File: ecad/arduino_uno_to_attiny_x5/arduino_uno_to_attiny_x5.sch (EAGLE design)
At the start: 3 parts

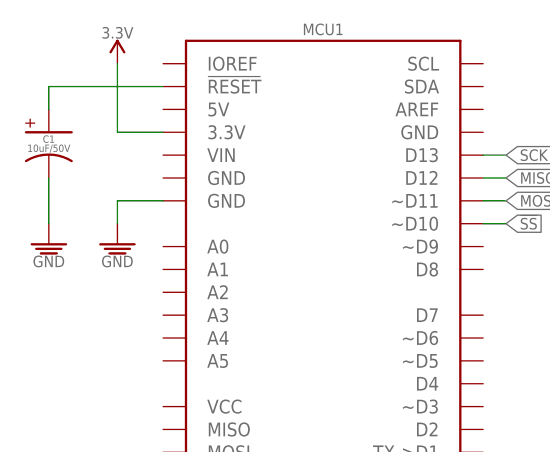
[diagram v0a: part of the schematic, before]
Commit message: Create schematic for pocket avr programmer (AVR ISP header) to ATtiny85.  Updated all schematics and their respective images.
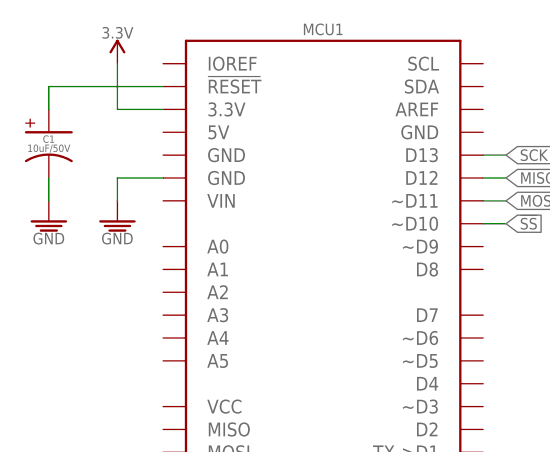
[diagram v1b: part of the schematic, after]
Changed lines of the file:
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@@
 <?xml version="1.0" encoding="utf-8"?>
 <!DOCTYPE eagle SYSTEM "eagle.dtd">
-<eagle version="9.1.1">
+<eagle version="9.1.3">
 <drawing>
 <settings>
@@
 <setting verticaltext="up"/>
 </settings>
-<grid distance="0.1" unitdist="inch" unit="inch" style="lines" multiple="1" display="yes" altdistance="0.01" altunitdist="inch" altunit="inch"/>
+<grid distance="0.1" unitdist="inch" unit="inch" style="lines" multiple="1" display="no" altdistance="0.01" altunitdist="inch" altunit="inch"/>
 <layers>
 <layer number="1" name="Top" color="4" fill="1" visible="no" active="no"/>
@@
 <instance part="MCU1" gate="G$1" x="38.1" y="35.56"/>
 <instance part="SUPPLY1" gate="GND" x="73.66" y="20.32"/>
-<instance part="SUPPLY2" gate="GND" x="15.24" y="40.64"/>
+<instance part="SUPPLY2" gate="GND" x="15.24" y="43.18"/>
 <instance part="SUPPLY3" gate="3.3V" x="15.24" y="60.96"/>
 <instance part="SUPPLY4" gate="3.3V" x="73.66" y="53.34"/>
 <instance part="C1" gate="G$1" x="7.62" y="53.34"/>
-<instance part="SUPPLY5" gate="GND" x="7.62" y="40.64"/>
+<instance part="SUPPLY5" gate="GND" x="7.62" y="43.18"/>
 </instances>
 <busses>
@@
 <segment>
 <pinref part="SUPPLY2" gate="GND" pin="GND"/>
-<wire x1="15.24" y1="43.18" x2="15.24" y2="45.72" width="0.1524" layer="91"/>
+<wire x1="15.24" y1="45.72" x2="15.24" y2="48.26" width="0.1524" layer="91"/>
 <pinref part="MCU1" gate="G$1" pin="GND@1"/>
-<wire x1="15.24" y1="45.72" x2="20.32" y2="45.72" width="0.1524" layer="91"/>
+<wire x1="15.24" y1="48.26" x2="20.32" y2="48.26" width="0.1524" layer="91"/>
 </segment>
 <segment>
 <pinref part="SUPPLY5" gate="GND" pin="GND"/>
 <pinref part="C1" gate="G$1" pin="K"/>
-<wire x1="7.62" y1="43.18" x2="7.62" y2="48.26" width="0.1524" layer="91"/>
+<wire x1="7.62" y1="45.72" x2="7.62" y2="48.26" width="0.1524" layer="91"/>
 </segment>
 </net>
@@
 <segment>
 <pinref part="MCU1" gate="G$1" pin="3.3V"/>
-<wire x1="20.32" y1="53.34" x2="15.24" y2="53.34" width="0.1524" layer="91"/>
-<wire x1="15.24" y1="53.34" x2="15.24" y2="60.96" width="0.1524" layer="91"/>
+<wire x1="20.32" y1="55.88" x2="15.24" y2="55.88" width="0.1524" layer="91"/>
+<wire x1="15.24" y1="55.88" x2="15.24" y2="60.96" width="0.1524" layer="91"/>
 <pinref part="SUPPLY3" gate="3.3V" pin="3.3V"/>
 </segment>
